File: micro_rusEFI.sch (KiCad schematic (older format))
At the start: 59 parts, among them J12 Conn_01x01, J13 Conn_01x01, J3 Conn_01x01, J4 Conn_02x05_Counter_Clockwise, J5 Conn_01x01, J6 Conn_01x01_Female, J8 Conn_01x01_Female, U3 molex_48pin_MRE, U7 XC6206 3.3V

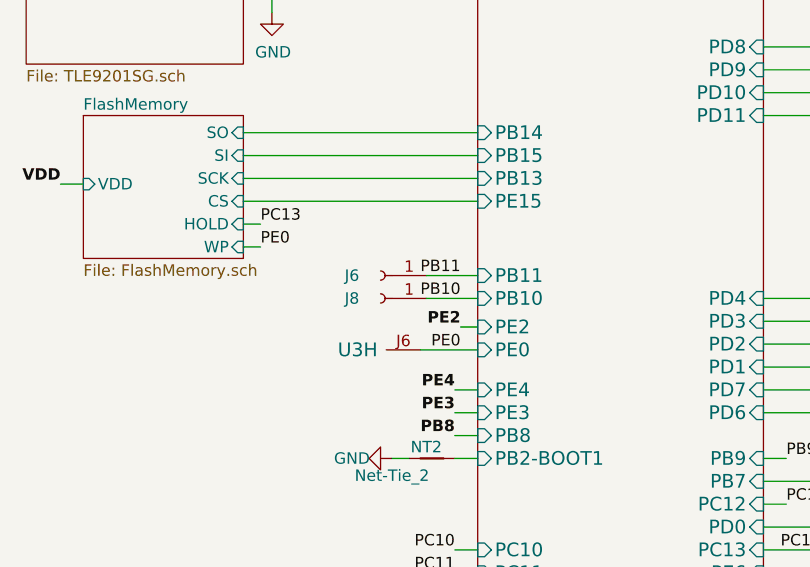
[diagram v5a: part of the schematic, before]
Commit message: J6 is now J12 J8 is now J13 Updated MRE footprint to include UART via's.
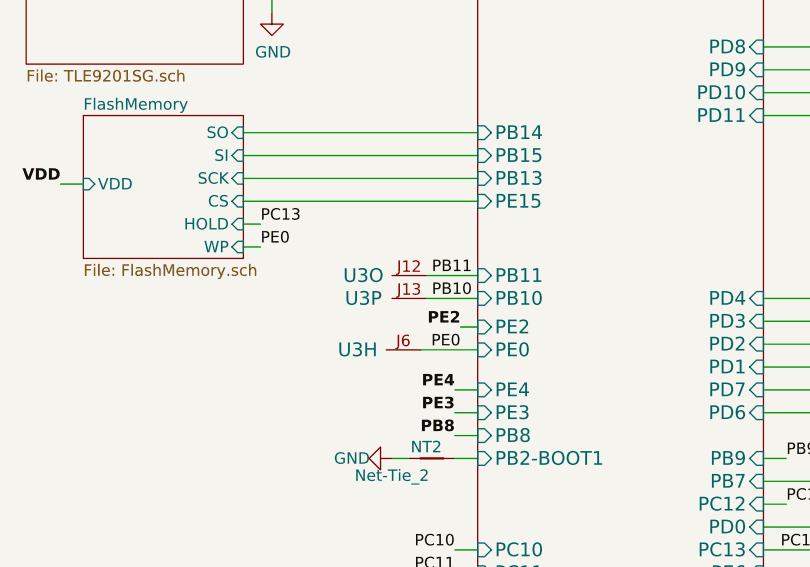
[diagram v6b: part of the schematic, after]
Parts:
- removed J6, J8: Conn_01x01_Female, Connector_PinHeader_1.00mm:PinHeader_1x01_P1.00mm_Vertical, symbol Connector:Conn_01x01_Female
- added unit 16 of U3
- added unit 15 of U3
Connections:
- net PB10: now also U3.J13
- net PB11: now also U3.J12
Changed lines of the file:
@@
 Wire Wire Line
 	5675 7900 5750 7900
-$Comp
-L Connector:Conn_01x01_Female J6
-U 1 1 5F134DAE
-P 6275 8025
-F 0 "J6" H 6400 8025 50  0000 C CNN
-F 1 "Conn_01x01_Female" H 6167 7891 50  0001 C CNN
-F 2 "Connector_PinHeader_1.00mm:PinHeader_1x01_P1.00mm_Vertical" H 6275 8025 50  0001 C CNN
-F 3 "~" H 6275 8025 50  0001 C CNN
-	1    6275 8025
-	-1   0    0    1
-$EndComp
-$Comp
-L Connector:Conn_01x01_Female J8
-U 1 1 5F199C4D
-P 6275 8125
-F 0 "J8" H 6400 8125 50  0000 C CNN
-F 1 "Conn_01x01_Female" H 6167 7991 50  0001 C CNN
-F 2 "Connector_PinHeader_1.00mm:PinHeader_1x01_P1.00mm_Vertical" H 6275 8125 50  0001 C CNN
-F 3 "~" H 6275 8125 50  0001 C CNN
-	1    6275 8125
-	-1   0    0    1
-$EndComp
 Wire Wire Line
 	6700 8025 6475 8025
 Wire Wire Line
 	6700 8125 6475 8125
-Text Label 6625 8125 2    50   ~ 0
+Text Label 6675 8125 2    50   ~ 0
 PB10
-Text Label 6625 8025 2    50   ~ 0
+Text Label 6675 8025 2    50   ~ 0
 PB11
+$Comp
+L rusefi_Molex_MRE_Connector:molex_48pin_MRE U3
+U 16 1 5F86BB48
+P 7025 8125
+F 0 "U3" H 7850 8125 60  0000 C CNN
+F 1 "molex_48pin_MRE" V 8206 8530 60  0001 C CNN
+F 2 "rusefi_lib:Molex_48_MRE" H 7025 8125 60  0001 C CNN
+F 3 "" H 7025 8125 60  0001 C CNN
+	16   7025 8125
+	-1   0    0    1
+$EndComp
+$Comp
+L rusefi_Molex_MRE_Connector:molex_48pin_MRE U3
+U 15 1 5F86E169
+P 7025 8025
+F 0 "U3" H 7850 8025 60  0000 C CNN
+F 1 "molex_48pin_MRE" V 8206 8430 60  0001 C CNN
+F 2 "rusefi_lib:Molex_48_MRE" H 7025 8025 60  0001 C CNN
+F 3 "" H 7025 8025 60  0001 C CNN
+	15   7025 8025
+	-1   0    0    1
+$EndComp
 $EndSCHEMATC
